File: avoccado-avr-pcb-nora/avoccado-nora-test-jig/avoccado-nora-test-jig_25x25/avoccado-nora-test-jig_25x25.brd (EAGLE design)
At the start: 25 x 25 mm, 24 parts

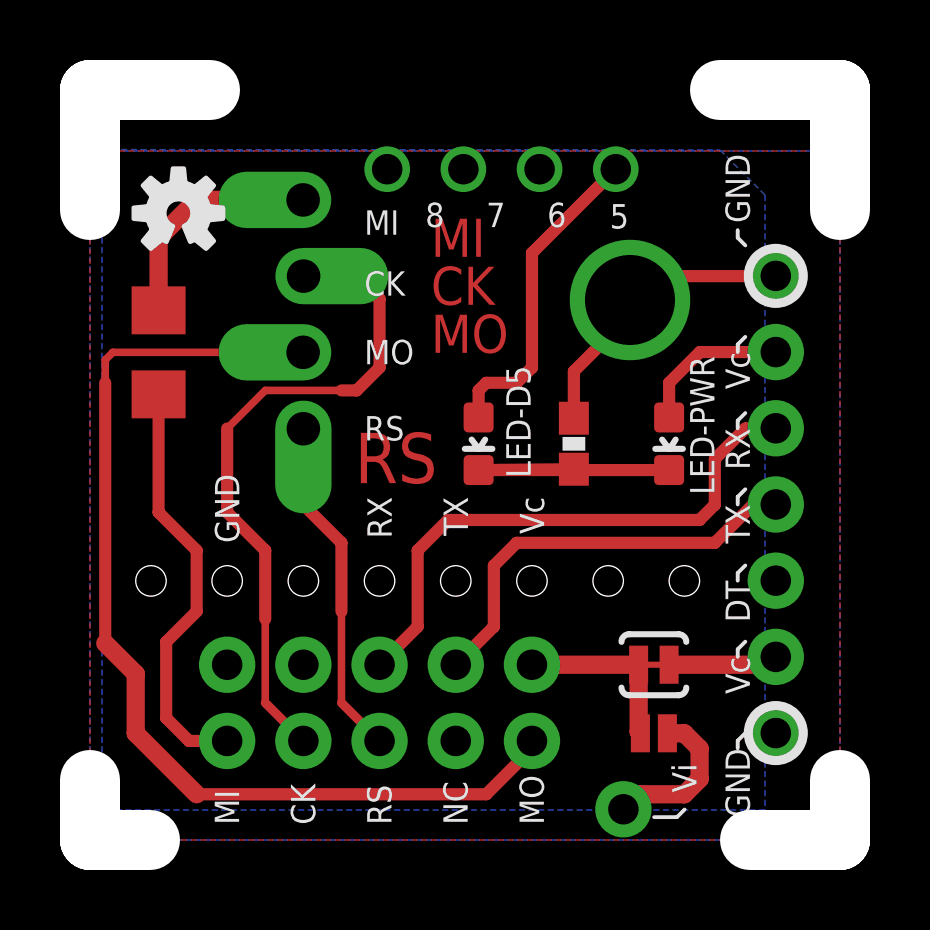
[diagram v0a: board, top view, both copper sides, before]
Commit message: test alignment of test jig panel
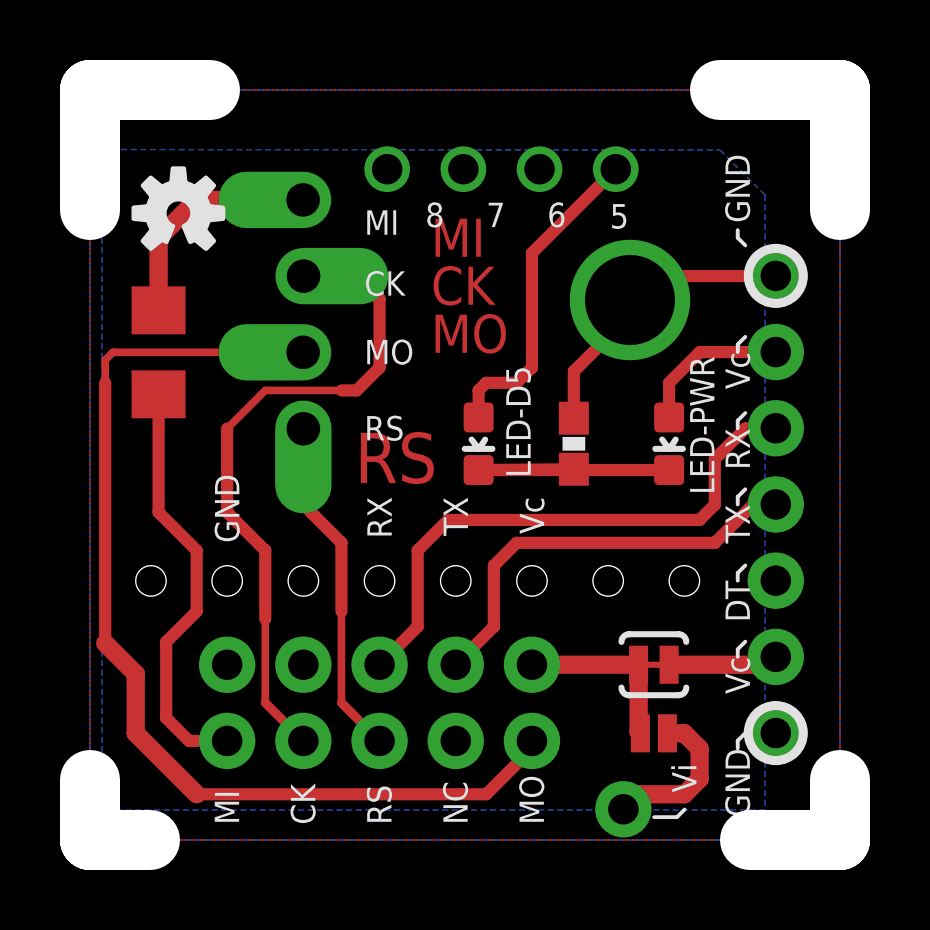
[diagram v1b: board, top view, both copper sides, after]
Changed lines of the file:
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@@
 <setting verticaltext="up"/>
 </settings>
-<grid distance="24.5" unitdist="mm" unit="mm" style="lines" multiple="1" display="yes" altdistance="0.1" altunitdist="mm" altunit="mm"/>
+<grid distance="0.02" unitdist="inch" unit="inch" style="lines" multiple="1" display="yes" altdistance="0.01" altunitdist="inch" altunit="inch"/>
 <layers>
 <layer number="1" name="Top" color="5" fill="1" visible="yes" active="yes"/>
@@
 <layer number="45" name="Holes" color="7" fill="1" visible="yes" active="yes"/>
 <layer number="46" name="Milling" color="3" fill="1" visible="yes" active="yes"/>
+<layer number="47" name="Measures" color="7" fill="1" visible="yes" active="yes"/>
+<layer number="48" name="Document" color="7" fill="1" visible="yes" active="yes"/>
+<layer number="49" name="Reference" color="7" fill="1" visible="yes" active="yes"/>
+<layer number="50" name="dxf" color="7" fill="1" visible="yes" active="yes"/>
 <layer number="51" name="tDocu" color="6" fill="1" visible="yes" active="yes"/>
 <layer number="52" name="bDocu" color="7" fill="1" visible="yes" active="yes"/>
 <layer number="53" name="tGND_GNDA" color="7" fill="9" visible="no" active="no"/>
 <layer number="54" name="bGND_GNDA" color="1" fill="9" visible="no" active="no"/>
+<layer number="56" name="wert" color="7" fill="1" visible="yes" active="yes"/>
 <layer number="57" name="tCAD" color="7" fill="1" visible="no" active="no"/>
 <layer number="90" name="Modules" color="5" fill="1" visible="no" active="no"/>
@@
 <layer number="99" name="SpiceOrder" color="7" fill="1" visible="no" active="no"/>
 <layer number="100" name="Muster" color="7" fill="1" visible="no" active="no"/>
+<layer number="101" name="Patch_Top" color="12" fill="4" visible="yes" active="yes"/>
+<layer number="102" name="Vscore" color="7" fill="1" visible="yes" active="yes"/>
+<layer number="103" name="tMap" color="7" fill="1" visible="yes" active="yes"/>
+<layer number="104" name="Name" color="7" fill="1" visible="yes" active="yes"/>
+<layer number="105" name="tPlate" color="7" fill="1" visible="yes" active="yes"/>
+<layer number="106" name="bPlate" color="7" fill="1" visible="yes" active="yes"/>
+<layer number="107" name="Crop" color="7" fill="1" visible="yes" active="yes"/>
+<layer number="108" name="tplace-old" color="10" fill="1" visible="yes" active="yes"/>
+<layer number="109" name="ref-old" color="11" fill="1" visible="yes" active="yes"/>
+<layer number="110" name="fp0" color="7" fill="1" visible="yes" active="yes"/>
+<layer number="111" name="LPC17xx" color="7" fill="1" visible="yes" active="yes"/>
+<layer number="112" name="tSilk" color="7" fill="1" visible="yes" active="yes"/>
+<layer number="113" name="IDFDebug" color="7" fill="1" visible="yes" active="yes"/>
+<layer number="116" name="Patch_BOT" color="9" fill="4" visible="yes" active="yes"/>
+<layer number="121" name="_tsilk" color="7" fill="1" visible="yes" active="yes"/>
+<layer number="122" name="_bsilk" color="7" fill="1" visible="yes" active="yes"/>
+<layer number="123" name="tTestmark" color="7" fill="1" visible="yes" active="yes"/>
+<layer number="124" name="bTestmark" color="7" fill="1" visible="yes" active="yes"/>
+<layer number="125" name="_tNames" color="7" fill="1" visible="yes" active="yes"/>
+<layer number="126" name="_bNames" color="7" fill="1" visible="yes" active="yes"/>
+<layer number="127" name="_tValues" color="7" fill="1" visible="yes" active="yes"/>
+<layer number="128" name="_bValues" color="7" fill="1" visible="yes" active="yes"/>
+<layer number="131" name="tAdjust" color="7" fill="1" visible="yes" active="yes"/>
+<layer number="132" name="bAdjust" color="7" fill="1" visible="yes" active="yes"/>
+<layer number="144" name="Drill_legend" color="7" fill="1" visible="yes" active="yes"/>
+<layer number="150" name="Notes" color="7" fill="1" visible="yes" active="yes"/>
+<layer number="151" name="HeatSink" color="7" fill="1" visible="yes" active="yes"/>
+<layer number="152" name="_bDocu" color="7" fill="1" visible="yes" active="yes"/>
+<layer number="153" name="FabDoc1" color="7" fill="1" visible="yes" active="yes"/>
+<layer number="154" name="FabDoc2" color="7" fill="1" visible="yes" active="yes"/>
+<layer number="155" name="FabDoc3" color="7" fill="1" visible="yes" active="yes"/>
+<layer number="199" name="Contour" color="7" fill="1" visible="yes" active="yes"/>
 <layer number="200" name="200bmp" color="1" fill="10" visible="no" active="no"/>
 <layer number="201" name="201bmp" color="2" fill="1" visible="no" active="no"/>
 <layer number="202" name="202bmp" color="3" fill="1" visible="no" active="no"/>
+<layer number="203" name="203bmp" color="4" fill="10" visible="yes" active="yes"/>
+<layer number="204" name="204bmp" color="5" fill="10" visible="yes" active="yes"/>
+<layer number="205" name="205bmp" color="6" fill="10" visible="yes" active="yes"/>
+<layer number="206" name="206bmp" color="7" fill="10" visible="yes" active="yes"/>
+<layer number="207" name="207bmp" color="8" fill="10" visible="yes" active="yes"/>
+<layer number="208" name="208bmp" color="9" fill="10" visible="yes" active="yes"/>
+<layer number="209" name="209bmp" color="7" fill="1" visible="yes" active="yes"/>
+<layer number="210" name="210bmp" color="7" fill="1" visible="yes" active="yes"/>
+<layer number="211" name="211bmp" color="7" fill="1" visible="yes" active="yes"/>
+<layer number="212" name="212bmp" color="7" fill="1" visible="yes" active="yes"/>
+<layer number="213" name="213bmp" color="7" fill="1" visible="yes" active="yes"/>
+<layer number="214" name="214bmp" color="7" fill="1" visible="yes" active="yes"/>
+<layer number="215" name="215bmp" color="7" fill="1" visible="yes" active="yes"/>
+<layer number="216" name="216bmp" color="7" fill="1" visible="yes" active="yes"/>
 <layer number="217" name="217bmp" color="18" fill="1" visible="no" active="no"/>
 <layer number="218" name="218bmp" color="19" fill="1" visible="no" active="no"/>
@@
 <layer number="223" name="223bmp" color="24" fill="1" visible="no" active="no"/>
 <layer number="224" name="224bmp" color="25" fill="1" visible="no" active="no"/>
+<layer number="248" name="Housing" color="7" fill="1" visible="yes" active="yes"/>
+<layer number="249" name="Edge" color="7" fill="1" visible="yes" active="yes"/>
 <layer number="250" name="Descript" color="3" fill="1" visible="no" active="no"/>
 <layer number="251" name="SMDround" color="12" fill="11" visible="no" active="no"/>
+<layer number="254" name="cooling" color="7" fill="1" visible="yes" active="yes"/>
 </layers>
 <board>
@@
 <polygon width="0.4064" layer="1" isolate="0.6096" orphans="yes">
 <vertex x="0" y="0"/>
-<vertex x="0" y="22.968"/>
-<vertex x="25" y="22.968"/>
+<vertex x="0" y="25"/>
+<vertex x="25" y="25"/>
 <vertex x="25" y="0"/>
 </polygon>
@@
 <polygon width="0.4064" layer="16" isolate="0.6096">
 <vertex x="25" y="0"/>
-<vertex x="25" y="22.968"/>
-<vertex x="0" y="22.968"/>
+<vertex x="25" y="25"/>
+<vertex x="0" y="25"/>
 <vertex x="0" y="0"/>
 </polygon>
@@
 <wire x1="14.732" y1="3.048" x2="13.208" y2="1.524" width="0.4064" layer="1"/>
 <wire x1="13.208" y1="1.524" x2="3.556" y2="1.524" width="0.4064" layer="1"/>
+<wire x1="3.556" y1="1.524" x2="2.54" y2="1.524" width="0" layer="19" extent="1-16"/>
 <wire x1="0.508" y1="6.556" x2="0.508" y2="15.24" width="0.4064" layer="1"/>
 <wire x1="0.762" y1="16.256" x2="5.08" y2="16.256" width="0.254" layer="1"/>
@@
 <wire x1="0.508" y1="15.24" x2="0.508" y2="16.002" width="0.254" layer="1"/>
 <wire x1="0.508" y1="16.002" x2="0.762" y2="16.256" width="0.254" layer="1"/>
+<wire x1="2.54" y1="1.524" x2="2.032" y2="1.524" width="0" layer="19" extent="1-16"/>
+<wire x1="2.032" y1="1.524" x2="1.524" y2="2.032" width="0" layer="19" extent="1-16"/>
+<wire x1="1.524" y1="2.032" x2="1.524" y2="3.556" width="0" layer="19" extent="1-16"/>
 <wire x1="1.524" y1="3.556" x2="1.524" y2="5.54" width="0.6096" layer="1"/>
 <wire x1="1.524" y1="5.54" x2="0.508" y2="6.556" width="0.6096" layer="1"/>
 <wire x1="1.524" y1="3.556" x2="3.556" y2="1.524" width="0.6096" layer="1"/>
+<wire x1="3.556" y1="1.524" x2="1.524" y2="3.556" width="0" layer="19" extent="1-16"/>
 </signal>
 <signal name="TXO">
